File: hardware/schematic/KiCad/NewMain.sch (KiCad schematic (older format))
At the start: 16 parts, among them J1 MDB, J2-1 Conn_01x01, J2-2 Conn_01x01, J2-3 Conn_01x01, J2-4 Conn_01x01, Q1 BC807, Q2 BC807, Q3 2N7002, U1 DC24V-DC5V

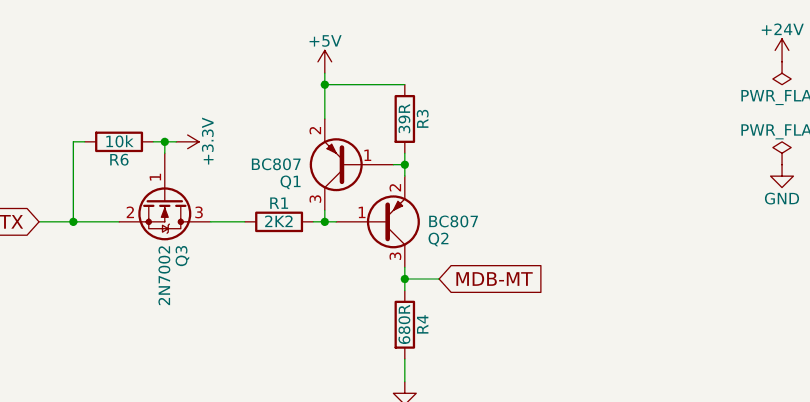
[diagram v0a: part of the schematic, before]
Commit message: correct transmit current 100ma
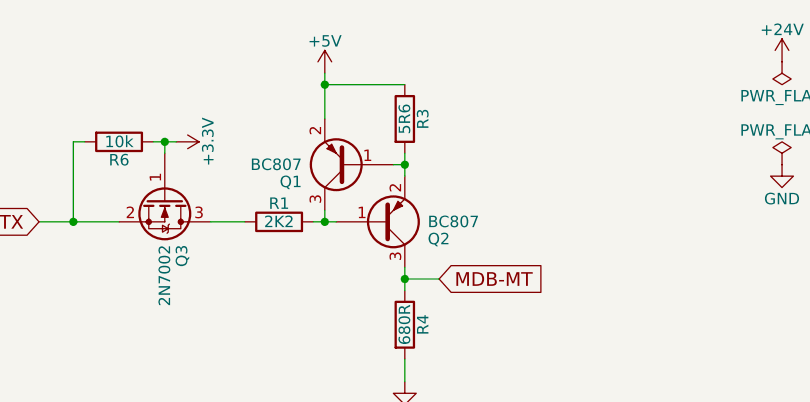
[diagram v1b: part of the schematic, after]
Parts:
- R3: value 39R -> 5R6
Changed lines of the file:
@@
 P 7600 1700
 F 0 "R3" V 7680 1700 50  0000 C CNN
-F 1 "39R" V 7600 1700 50  0000 C CNN
+F 1 "5R6" V 7600 1700 50  0000 C CNN
 F 2 "Resistors_SMD:R_0603_HandSoldering" V 7530 1700 50  0001 C CNN
 F 3 "" H 7600 1700 50  0001 C CNN
